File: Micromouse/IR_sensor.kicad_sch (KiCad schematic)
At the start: 36 parts, among them J11 IR_1, J12 IR_3, J13 IR_2, J14 IR_4, Q2 AO3400A, Q3 AO3400A, Q4 SFH_309FA, Q5 SFH_309FA, Q6 AO3400A, Q7 AO3400A, Q8 SFH_309FA, Q9 SFH_309FA

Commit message: Commit4
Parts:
- renumbered C32 to C57, C33 to C58, C34 to C59, C35 to C60, C36 to C61, C37 to C62, C38 to C63, C39 to C64, D12 to D18, D13 to D19, D14 to D20, D15 to D21, Q8 to Q10, Q9 to Q11, Q2 to Q4, Q3 to Q5, Q4 to Q6, Q5 to Q7, Q6 to Q8, Q7 to Q9, R27 to R39, R28 to R40, R29 to R41, R30 to R42, R31 to R43, R32 to R44, R33 to R45, R34 to R46, R35 to R47, R36 to R48, R37 to R49, R38 to R50

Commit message: Chasis minisumo terminado
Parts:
- removed D18, D19, D20, D21: SFH_4550, SFH4550:DIO_SFH_4550, symbol SFH_4550:SFH_4550
- removed Q10, Q11, Q6, Q7: SFH_309FA, SFH309FA:XDCR_SFH_309-4_5, symbol SFH_309-4_5:SFH_309-4_5
- added D18, D19, D20, D21: SFH-4550, LED_THT:LED_D5.0mm_Clear, symbol Device:LED
- added Q10, Q11, Q6, Q7: ST-1KL3A, LED_THT:LED_D5.0mm_IRBlack, symbol Device:Q_Photo_NPN
- C55: renamed from C57; footprint Capacitor_SMD:C_1206_3216Metric -> Capacitor_SMD:C_0402_1005Metric_Pad0.74x0.62mm_HandSolder
- C56: renamed from C58; footprint Capacitor_SMD:C_1206_3216Metric -> Capacitor_SMD:C_0402_1005Metric_Pad0.74x0.62mm_HandSolder
- C57: renamed from C59; footprint Capacitor_SMD:C_0201_0603Metric -> Capacitor_SMD:C_0402_1005Metric_Pad0.74x0.62mm_HandSolder
- C58: renamed from C60; footprint Capacitor_SMD:C_0201_0603Metric -> Capacitor_SMD:C_0402_1005Metric_Pad0.74x0.62mm_HandSolder
- C59: renamed from C61; footprint Capacitor_SMD:C_1206_3216Metric -> Capacitor_SMD:C_0402_1005Metric_Pad0.74x0.62mm_HandSolder
- C60: renamed from C62; footprint Capacitor_SMD:C_1206_3216Metric -> Capacitor_SMD:C_0402_1005Metric_Pad0.74x0.62mm_HandSolder
- C61: renamed from C63; footprint Capacitor_SMD:C_0201_0603Metric -> Capacitor_SMD:C_0402_1005Metric_Pad0.74x0.62mm_HandSolder
- C62: renamed from C64; footprint Capacitor_SMD:C_0201_0603Metric -> Capacitor_SMD:C_0402_1005Metric_Pad0.74x0.62mm_HandSolder
- J14: renamed from J11; footprint (none) -> MicromouseHuellas:IR_SENSOR_PAD_HIJO
- J15: renamed from J12; footprint (none) -> MicromouseHuellas:IR_SENSOR_PAD_HIJO
- J16: renamed from J13; footprint (none) -> MicromouseHuellas:IR_SENSOR_PAD_HIJO
- J17: renamed from J14; footprint (none) -> MicromouseHuellas:IR_SENSOR_PAD_HIJO
- R39, R40, R45, R46: footprint Resistor_SMD:R_0201_0603Metric -> Resistor_SMD:R_0402_1005Metric_Pad0.72x0.64mm_HandSolder
- R41, R42, R47, R48: value 30 -> 20; footprint Resistor_SMD:R_0805_2012Metric -> Resistor_SMD:R_0805_2012Metric_Pad1.20x1.40mm_HandSolder
- R43, R44, R49, R50: value 1.5k -> 3.3k; footprint Resistor_SMD:R_0201_0603Metric -> Resistor_SMD:R_0402_1005Metric_Pad0.72x0.64mm_HandSolder
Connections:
- net +3V0_1: now also Q6.1 (C)
- net +3V0_2: now also Q10.1 (C)
- net +3V0_3: now also Q7.1 (C)
- net +3V0_4: now also Q11.1 (C)
- net IR_REC_1: now also Q6.2 (E)
- net IR_REC_2: now also Q10.2 (E)
- net IR_REC_3: now also Q7.2 (E)
- net IR_REC_4: now also Q11.2 (E)
- net at Q5.3 (D): now also D19.1 (K)
- net at R48.1: now also D21.2 (A)
- net at R42.1: now also D19.2 (A)
- net at Q9.3 (D): now also D21.1 (K)
- net at R41.1: now also D18.2 (A)
- net at R47.1: now also D20.2 (A)
- net at Q4.3 (D): now also D18.1 (K)
- net at Q8.3 (D): now also D20.1 (K)

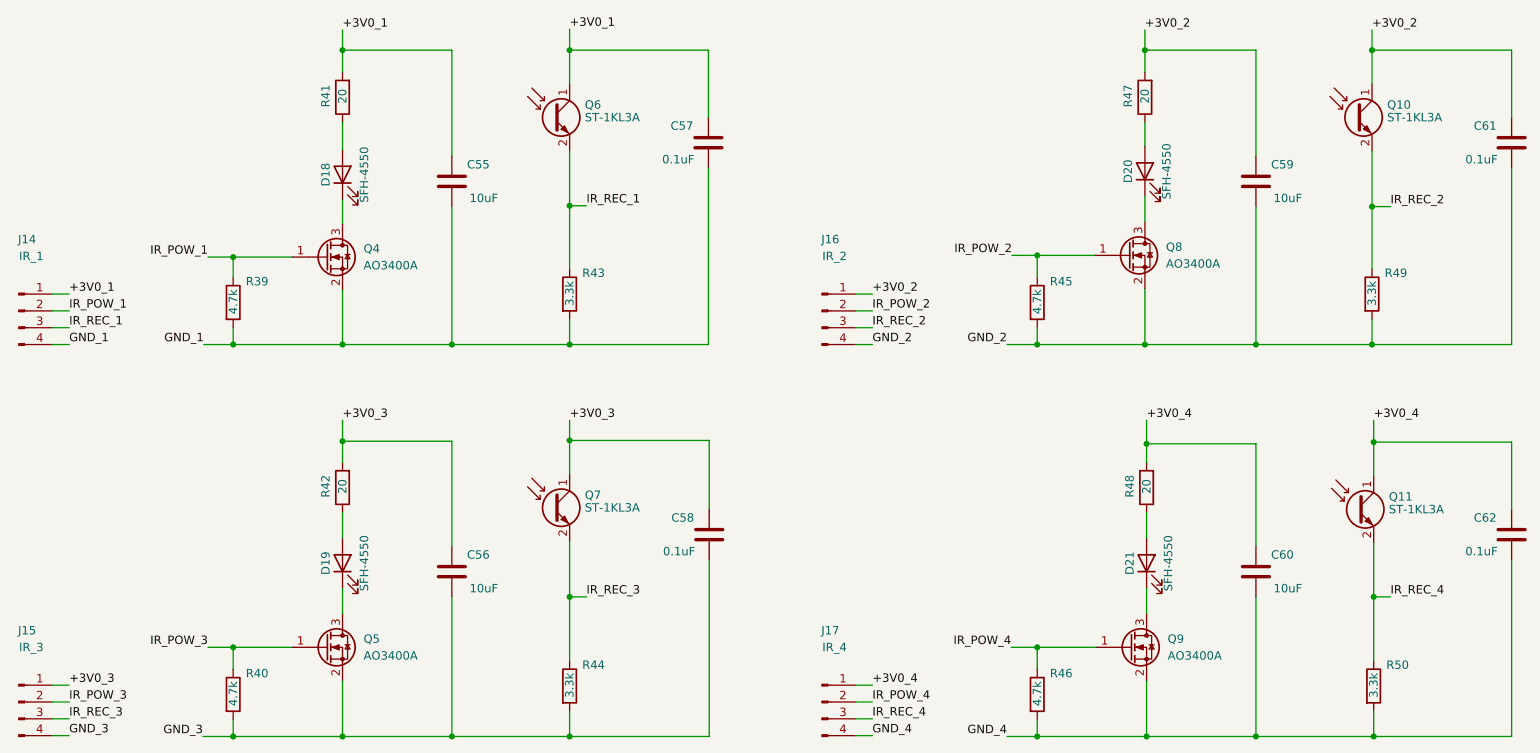
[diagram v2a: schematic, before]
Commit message: Red 3V0 cambiada a 3V3
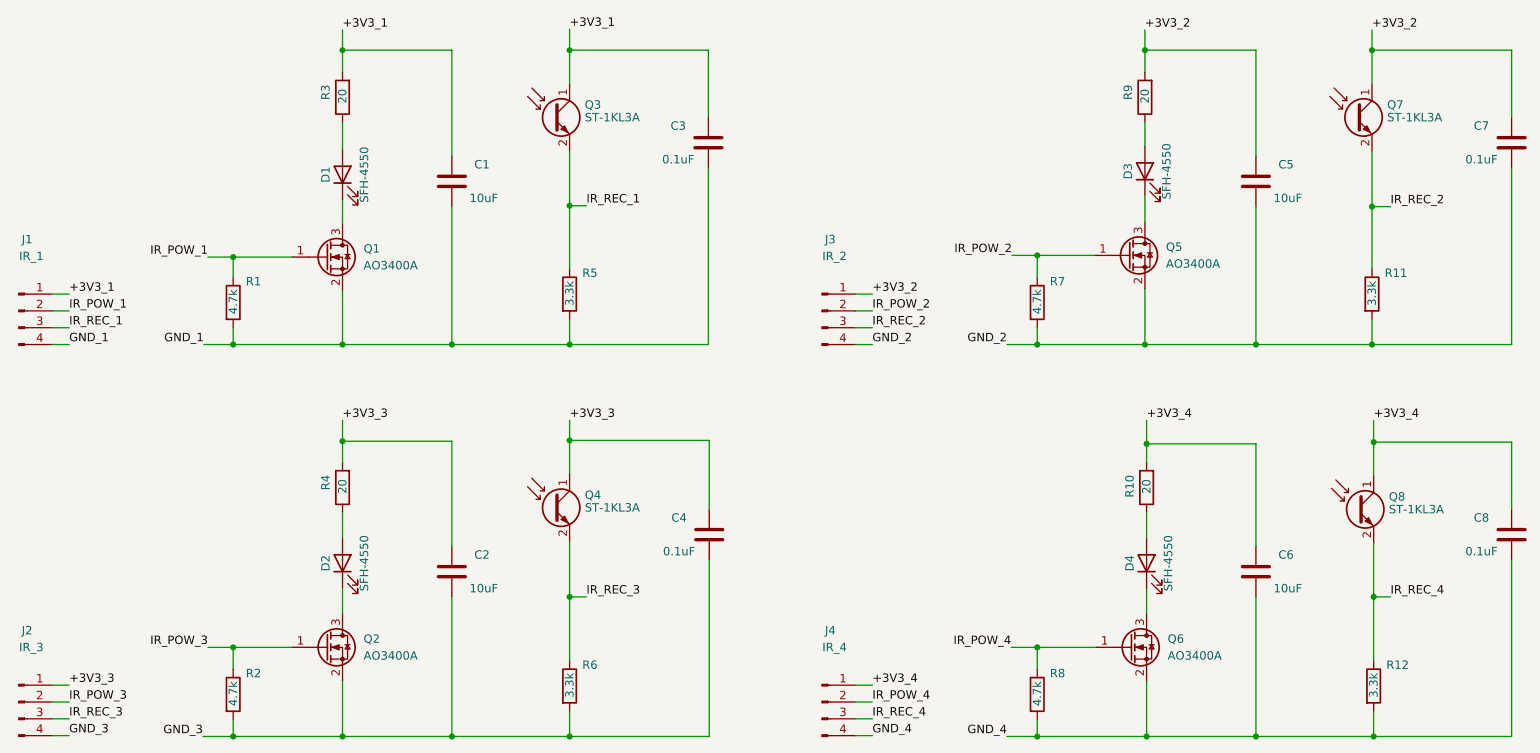
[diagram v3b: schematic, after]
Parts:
- renumbered C55 to C1, C56 to C2, C57 to C3, C58 to C4, C59 to C5, C60 to C6, C61 to C7, C62 to C8, D18 to D1, D19 to D2, D20 to D3, D21 to D4, J14 to J1, J15 to J2, J16 to J3, J17 to J4, Q4 to Q1, Q5 to Q2, Q6 to Q3, Q7 to Q4, Q8 to Q5, Q9 to Q6, Q10 to Q7, Q11 to Q8, R39 to R1, R48 to R10, R49 to R11, R50 to R12, R40 to R2, R41 to R3, R42 to R4, R43 to R5, R44 to R6, R45 to R7, R46 to R8, R47 to R9
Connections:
- net +3V0_1 renamed +3V3_1
- net +3V0_2 renamed +3V3_2
- net +3V0_3 renamed +3V3_3
- net +3V0_4 renamed +3V3_4

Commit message: Modelos 3D agregados
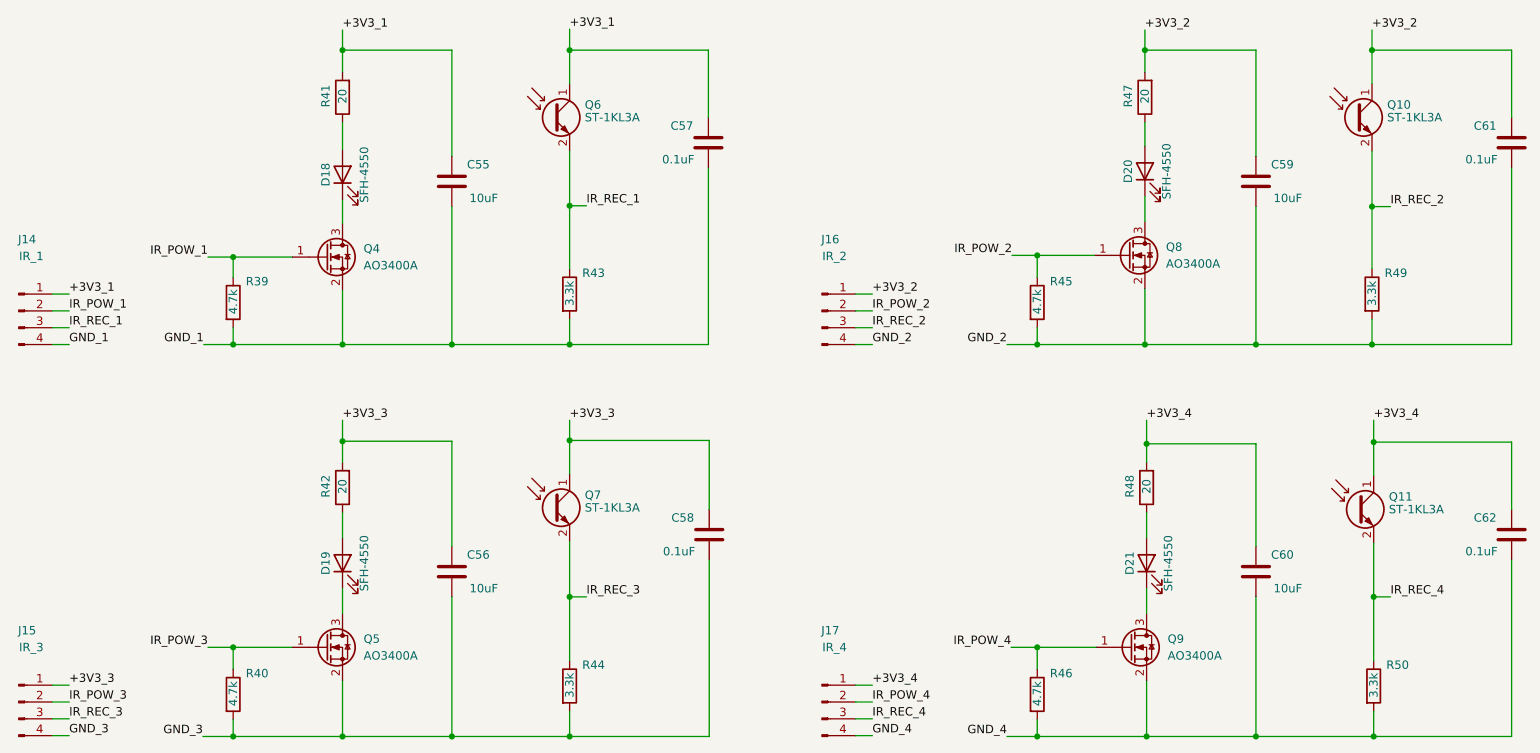
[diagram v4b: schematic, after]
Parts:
- renumbered C1 to C55, C2 to C56, C3 to C57, C4 to C58, C5 to C59, C6 to C60, C7 to C61, C8 to C62, D1 to D18, D2 to D19, D3 to D20, D4 to D21, J1 to J14, J2 to J15, J3 to J16, J4 to J17, Q7 to Q10, Q8 to Q11, Q1 to Q4, Q2 to Q5, Q3 to Q6, Q4 to Q7, Q5 to Q8, Q6 to Q9, R1 to R39, R2 to R40, R3 to R41, R4 to R42, R5 to R43, R6 to R44, R7 to R45, R8 to R46, R9 to R47, R10 to R48, R11 to R49, R12 to R50
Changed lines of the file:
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@@
 		(on_board yes)
 		(dnp no)
-		(property "Reference" "R5"
+		(property "Reference" "R43"
 			(at 118.745 69.215 0)
 			(effects
@@
 		(on_board yes)
 		(dnp no)
-		(property "Reference" "R1"
+		(property "Reference" "R39"
 			(at 67.945 70.485 0)
 			(effects
@@
 		(on_board yes)
 		(dnp no)
-		(property "Reference" "Q4"
+		(property "Reference" "Q7"
 			(at 119.126 103.4796 0)
 			(effects
@@
 		(on_board yes)
 		(dnp no)
-		(property "Reference" "C2"
+		(property "Reference" "C56"
 			(at 104.775 111.76 0)
 			(effects
@@
 		(on_board yes)
 		(dnp no)
-		(property "Reference" "C6"
+		(property "Reference" "C60"
 			(at 226.187 111.76 0)
 			(effects
@@
 		(on_board yes)
 		(dnp no)
-		(property "Reference" "R8"
+		(property "Reference" "R46"
 			(at 189.357 129.667 0)
 			(effects
@@
 		(dnp no)
 		(fields_autoplaced yes)
-		(property "Reference" "Q2"
+		(property "Reference" "Q5"
 			(at 85.725 124.4599 0)
 			(effects
@@
 		(on_board yes)
 		(dnp no)
-		(property "Reference" "R10"
+		(property "Reference" "R48"
 			(at 201.422 99.695 90)
 			(effects
@@
 		(on_board yes)
 		(dnp no)
-		(property "Reference" "D1"
+		(property "Reference" "D18"
 			(at 80.01 54.356 0)
 			(effects
@@
 		(on_board yes)
 		(dnp no)
-		(property "Reference" "D3"
+		(property "Reference" "D20"
 			(at 201.168 53.848 0)
 			(effects
@@
 		(on_board yes)
 		(dnp no)
-		(property "Reference" "R4"
+		(property "Reference" "R42"
 			(at 80.01 99.695 90)
 			(effects
@@
 		(on_board yes)
 		(dnp no)
-		(property "Reference" "R12"
+		(property "Reference" "R50"
 			(at 240.157 128.397 0)
 			(effects
@@
 		(on_board yes)
 		(dnp no)
-		(property "Reference" "C8"
+		(property "Reference" "C62"
 			(at 253.365 106.172 0)
 			(effects
@@
 		(on_board yes)
 		(dnp no)
-		(property "Reference" "J4"
+		(property "Reference" "J17"
 			(at 156.21 123.19 0)
 			(effects
@@
 		(on_board yes)
 		(dnp no)
-		(property "Reference" "J2"
+		(property "Reference" "J15"
 			(at 34.925 123.19 0)
 			(effects
@@
 		(on_board yes)
 		(dnp no)
-		(property "Reference" "C5"
+		(property "Reference" "C59"
 			(at 226.187 52.832 0)
 			(effects
@@
 		(dnp no)
 		(fields_autoplaced yes)
-		(property "Reference" "Q6"
+		(property "Reference" "Q9"
 			(at 207.137 124.4599 0)
 			(effects
@@
 		(on_board yes)
 		(dnp no)
-		(property "Reference" "R3"
+		(property "Reference" "R41"
 			(at 80.01 40.767 90)
 			(effects
@@
 		(on_board yes)
 		(dnp no)
-		(property "Reference" "J1"
+		(property "Reference" "J14"
 			(at 34.925 64.135 0)
 			(effects
@@
 		(on_board yes)
 		(dnp no)
-		(property "Reference" "Q8"
+		(property "Reference" "Q11"
 			(at 240.538 103.7336 0)
 			(effects
@@
 		(on_board yes)
 		(dnp no)
-		(property "Reference" "R2"
+		(property "Reference" "R40"
 			(at 67.945 129.667 0)
 			(effects
@@
 		(on_board yes)
 		(dnp no)
-		(property "Reference" "D2"
+		(property "Reference" "D19"
 			(at 80.01 113.03 0)
 			(effects
@@
 		(on_board yes)
 		(dnp no)
-		(property "Reference" "J3"
+		(property "Reference" "J16"
 			(at 156.21 64.135 0)
 			(effects
@@
 		(on_board yes)
 		(dnp no)
-		(property "Reference" "R9"
+		(property "Reference" "R47"
 			(at 201.168 40.767 90)
 			(effects
@@
 		(on_board yes)
 		(dnp no)
-		(property "Reference" "C3"
+		(property "Reference" "C57"
 			(at 132.08 46.99 0)
 			(effects
@@
 		(on_board yes)
 		(dnp no)
-		(property "Reference" "D4"
+		(property "Reference" "D21"
 			(at 201.422 113.03 0)
 			(effects
@@
 		(dnp no)
 		(fields_autoplaced yes)
-		(property "Reference" "Q1"
+		(property "Reference" "Q4"
 			(at 85.725 65.5319 0)
 			(effects
@@
 		(on_board yes)
 		(dnp no)
-		(property "Reference" "R11"
+		(property "Reference" "R49"
 			(at 239.903 69.215 0)
 			(effects
@@
 		(on_board yes)
 		(dnp no)
-		(property "Reference" "R7"
+		(property "Reference" "R45"
 			(at 189.357 70.485 0)
 			(effects
@@
 		(on_board yes)
 		(dnp no)
-		(property "Reference" "Q7"
+		(property "Reference" "Q10"
 			(at 240.284 44.5516 0)
 			(effects
@@
 		(on_board yes)
 		(dnp no)
-		(property "Reference" "Q3"
+		(property "Reference" "Q6"
 			(at 119.126 44.5516 0)
 			(effects
@@
 		(dnp no)
 		(fields_autoplaced yes)
-		(property "Reference" "Q5"
+		(property "Reference" "Q8"
 			(at 206.883 65.2779 0)
 			(effects
@@
 		(on_board yes)
 		(dnp no)
-		(property "Reference" "R6"
+		(property "Reference" "R44"
 			(at 118.745 128.397 0)
 			(effects
@@
 		(on_board yes)
 		(dnp no)
-		(property "Reference" "C4"
+		(property "Reference" "C58"
 			(at 132.207 106.172 0)
 			(effects
@@
 		(on_board yes)
 		(dnp no)
-		(property "Reference" "C1"
+		(property "Reference" "C55"
 			(at 104.775 52.832 0)
 			(effects
@@
 		(on_board yes)
 		(dnp no)
-		(property "Reference" "C7"
+		(property "Reference" "C61"
 			(at 253.365 46.99 0)
 			(effects
